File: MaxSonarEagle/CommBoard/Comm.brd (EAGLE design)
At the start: 160 x 100 mm, 1 part

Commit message: schematic updates
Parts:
- added S1, S2: (no value), SparkFun-Switches:DIPSWITCH-08
- added U$1, U$2, U$3, U$4, U$5, U$6, U$7, U$8: LV-MAXSONAR-EZ, Comm:1X07
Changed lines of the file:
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@@
 <layer number="230" name="230bmp" color="7" fill="1" visible="yes" active="yes"/>
 <layer number="231" name="231bmp" color="7" fill="1" visible="yes" active="yes"/>
+<layer number="232" name="Eagle3D_PG2" color="7" fill="1" visible="no" active="no"/>
+<layer number="233" name="Eagle3D_PG3" color="7" fill="1" visible="no" active="no"/>
 <layer number="248" name="Housing" color="7" fill="1" visible="yes" active="yes"/>
 <layer number="249" name="Edge" color="7" fill="1" visible="yes" active="yes"/>
@@
 <elements>
 <element name="FRAME1" library="SparkFun-Aesthetics" package="CREATIVE_COMMONS" value="FRAME-LEDGER" x="21.59" y="-8.89"/>
+<element name="U$1" library="Comm" package="1X07" value="LV-MAXSONAR-EZ" x="10.16" y="-20.32"/>
+<element name="U$2" library="Comm" package="1X07" value="LV-MAXSONAR-EZ" x="10.16" y="-39.37"/>
+<element name="U$3" library="Comm" package="1X07" value="LV-MAXSONAR-EZ" x="10.16" y="-58.42"/>
+<element name="U$4" library="Comm" package="1X07" value="LV-MAXSONAR-EZ" x="10.16" y="-77.47"/>
+<element name="U$5" library="Comm" package="1X07" value="LV-MAXSONAR-EZ" x="10.16" y="-96.52"/>
+<element name="U$6" library="Comm" package="1X07" value="LV-MAXSONAR-EZ" x="10.16" y="-115.57"/>
+<element name="U$7" library="Comm" package="1X07" value="LV-MAXSONAR-EZ" x="10.16" y="-134.62"/>
+<element name="U$8" library="Comm" package="1X07" value="LV-MAXSONAR-EZ" x="10.16" y="-153.67"/>
+<element name="S1" library="SparkFun-Switches" package="DIPSWITCH-08" value="" x="16.51" y="-175.26">
+<attribute name="PROD_ID" value="SWCH-12197" x="16.51" y="-175.26" size="1.778" layer="27" display="off"/>
+<attribute name="SF_SKU" value="COM-08034" x="16.51" y="-175.26" size="1.778" layer="27" display="off"/>
+</element>
+<element name="S2" library="SparkFun-Switches" package="DIPSWITCH-08" value="" x="16.51" y="-198.12">
+<attribute name="PROD_ID" value="SWCH-12197" x="16.51" y="-198.12" size="1.778" layer="27" display="off"/>
+<attribute name="SF_SKU" value="COM-08034" x="16.51" y="-198.12" size="1.778" layer="27" display="off"/>
+</element>
 </elements>
 <signals>

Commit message: finalized board
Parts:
- removed S1: (no value), SparkFun-Switches:DIPSWITCH-08
- added D1, D11, D13, D15, D3, D33, D37, D5, D7, D9: (no value), SparkFun-LED:LED-0603
- added H1, H2, H3, H4: STAND-OFF, SparkFun-Hardware:STAND-OFF
- added J2: (no value), SparkFun-Connectors:MOLEX-1X6
- added Q1, Q10, Q19, Q2, Q21, Q22, Q23, Q24, Q25, Q26, Q27, Q3, Q4, Q5, Q6, Q7, Q8, Q9: 2N3904, SparkFun-DiscreteSemi:SOT23-3
- added R1, R11, R13, R15, R3, R33, R5, R7, R9: 50, SparkFun-Resistors:0805
- added R10, R12, R14, R16, R17, R18, R2, R38, R4, R42, R44, R46, R48, R50, R52, R54, R6, R8: 1k, SparkFun-Resistors:0805
- added R19, R49: 10k, SparkFun-Resistors:0805
- added R37: 350, SparkFun-Resistors:0805
- added U1, U2: 74HC1G04, SparkFun-IC-Logic:SOT353
- moved S2 241.2 mm to (71.1, 36.8), turned to 270 degrees
- moved U$8 186.7 mm to (58.4, 26.7), turned to 270 degrees
- moved U$7 166.3 mm to (50.8, 26.7), turned to 270 degrees
- moved U$6 146.0 mm to (43.2, 26.7), turned to 270 degrees
- moved U$5 125.8 mm to (35.6, 26.7), turned to 270 degrees
- moved U$4 105.6 mm to (27.9, 26.7), turned to 270 degrees
- moved FRAME1 92.0 mm to (99.1, 40.6), turned to 180 degrees
- moved U$3 85.7 mm to (20.3, 26.7), turned to 270 degrees
- moved U$2 66.1 mm to (12.7, 26.7), turned to 270 degrees
- moved U$1 47.3 mm to (5.08, 26.7), turned to 270 degrees
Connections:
- new net GND: J2.1, Q1.2, Q10.2, Q3.2, Q4.2, Q5.2, Q6.2, Q7.2, Q8.2, Q9.2, R19.1, R37.1, R49.1, U$1.1, U$1.7, U$2.1, U$2.7, U$3.1, U$3.7, U$4.1, U$4.7, U$5.1, U$5.7, U$6.1, U$6.7, U$7.1, U$7.7, U$8.1, U$8.7, U1.3, U2.3
- new net IO-UART-RX: J2.5, U1.4
- new net IO-UART-TX: J2.4, U2.2
- new net IOTX: Q2.2, R19.2, R2.1, S2.1, U$1.4
- new net N$1: D1.C, R1.2
- new net N$10: Q6.3, R9.1
- new net N$11: D11.C, R11.2
- new net N$12: Q7.3, R11.1
- new net N$13: D13.C, R13.2
- new net N$14: Q8.3, R13.1
- new net N$15: D15.C, R15.2
- new net N$16: Q9.3, R15.1
- new net N$17: Q2.1, R17.2
- new net N$18: Q10.3, R33.1
- new net N$2: Q1.3, R1.1
- new net N$20: Q10.1, R2.2
- new net N$22: Q9.1, R4.2
- new net N$24: Q8.1, R6.2
- new net N$26: Q7.1, R8.2
- new net N$28: Q6.1, R10.2
- new net N$3: D3.C, R3.2
- new net N$30: Q5.1, R12.2
- new net N$32: Q1.1, R14.2
- new net N$33: D33.C, R33.2
- new net N$34: Q3.1, R16.2
- new net N$37: D37.C, R37.2
- new net N$38: Q19.1, R38.2
- new net N$4: Q3.3, R3.1
- new net N$5: D5.C, R5.2
- new net N$6: Q4.3, R5.1
- new net N$61: Q21.1, R42.2
- new net N$63: Q4.1, R18.2
- new net N$65: Q22.1, R44.2
- new net N$68: Q23.1, R46.2
- new net N$7: D7.C, R7.2
- new net N$71: Q24.1, R48.2
- new net N$74: Q25.1, R50.2
- new net N$77: Q26.1, R52.2
- new net N$8: Q5.3, R7.1
- new net N$80: Q27.1, R54.2
- new net N$9: D9.C, R9.2
- new net RS232-RX: Q19.2, Q21.2, Q22.2, Q23.2, Q24.2, Q25.2, Q26.2, Q27.2, R49.2, U1.2
- new net RS232-TX: R17.1, U2.4
- new net TX1: R14.1, R38.1, S2.16, S2.2, U$1.3, U$2.4
- new net TX2: R16.1, R42.1, S2.15, S2.3, U$2.3, U$3.4
- new net TX3: R18.1, R44.1, S2.14, S2.4, U$3.3, U$4.4
- new net TX4: R12.1, R46.1, S2.13, S2.5, U$4.3, U$5.4
- new net TX5: R10.1, R48.1, S2.12, S2.6, U$5.3, U$6.4
- new net TX6: R50.1, R8.1, S2.11, S2.7, U$6.3, U$7.4
- new net TX7: R52.1, R6.1, S2.10, S2.8, U$7.3, U$8.4
- new net TX8: R4.1, R54.1, S2.9, U$8.3
- new net VIN: D1.A, D11.A, D13.A, D15.A, D3.A, D33.A, D37.A, D5.A, D7.A, D9.A, J2.3, Q19.3, Q2.3, Q21.3, Q22.3, Q23.3, Q24.3, Q25.3, Q26.3, Q27.3, U$1.2, U$2.2, U$3.2, U$4.2, U$5.2, U$6.2, U$7.2, U$8.2, U1.5, U2.5
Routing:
- net IOTX: track 0.00 -> 230.1 mm
- net VIN: track 0.00 -> 183.6 mm, vias 0 -> 14
- net TX1: track 0.00 -> 132.4 mm
- net RS232-RX: track 0.00 -> 130.8 mm, vias 0 -> 2
- net TX2: track 0.00 -> 100.0 mm
- net TX3: track 0.00 -> 93.8 mm
- net TX4: track 0.00 -> 88.8 mm
- net TX5: track 0.00 -> 81.7 mm, vias 0 -> 1
- net TX6: track 0.00 -> 74.9 mm
- net TX7: track 0.00 -> 70.0 mm
- net TX8: track 0.00 -> 59.3 mm, vias 0 -> 3
- net GND: track 0.00 -> 51.4 mm, vias 0 -> 10
- net RS232-TX: track 0.00 -> 12.3 mm
- net N$16: track 0.00 -> 11.8 mm
- net N$14: track 0.00 -> 10.6 mm
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- added copper zone on layer 16, net GND
- added copper zone on layer 1, net VIN
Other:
- board size 160 x 100 mm -> 102.8 x 54.3 mm
- board text added: "+"
- board text added: "1"
- board text added: "1 2 3 4 5 6 7 8"
- board text added: "2"
- board text added: "3"
- board text added: "4"
- board text added: "5"
- board text added: "6"
- board text added: "7"
- board text added: "8"
- board text added: "GND"
- board text added: "IO"
- board text added: "S1 S2 S3 S4 S5 S6 S7 S8"
- board text added: "Sonar Communications Board v1.0"
- board text added: "TX Bridge"

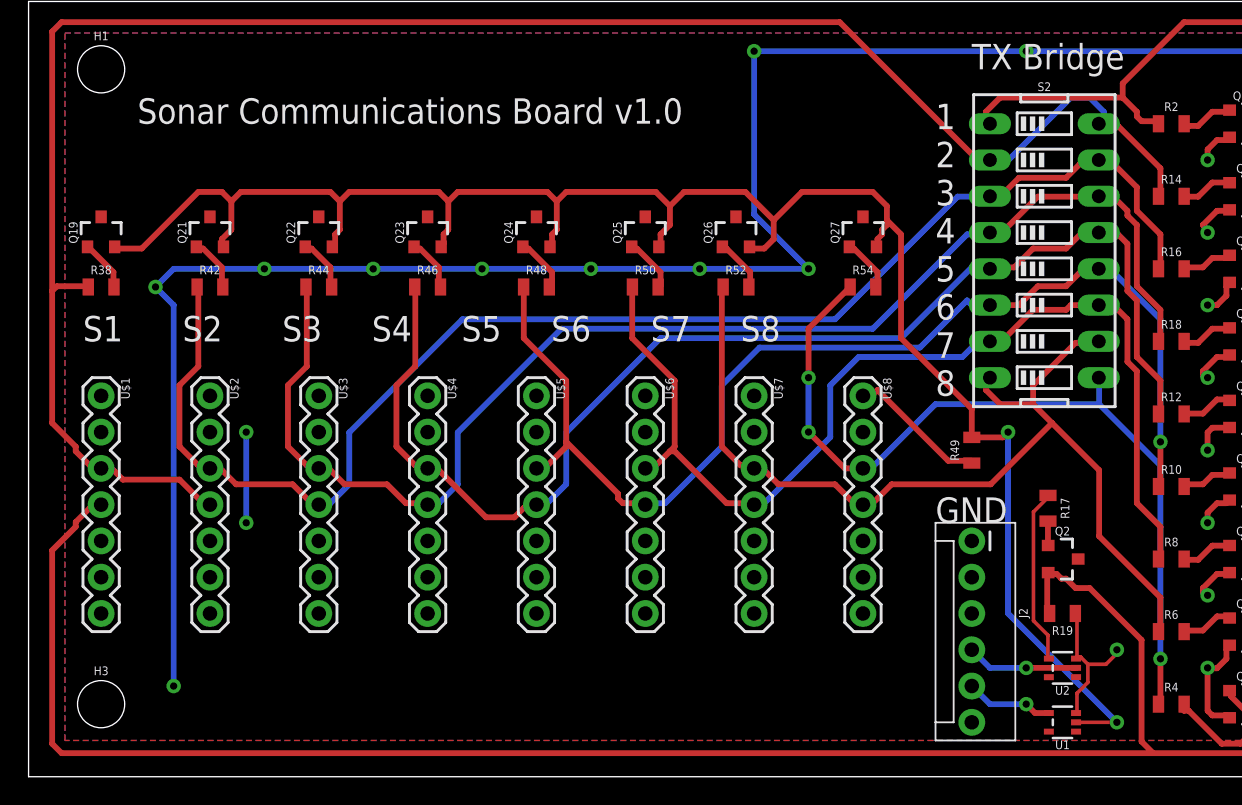
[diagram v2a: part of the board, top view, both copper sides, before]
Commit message: added pulldown resistors to sonar rx lines
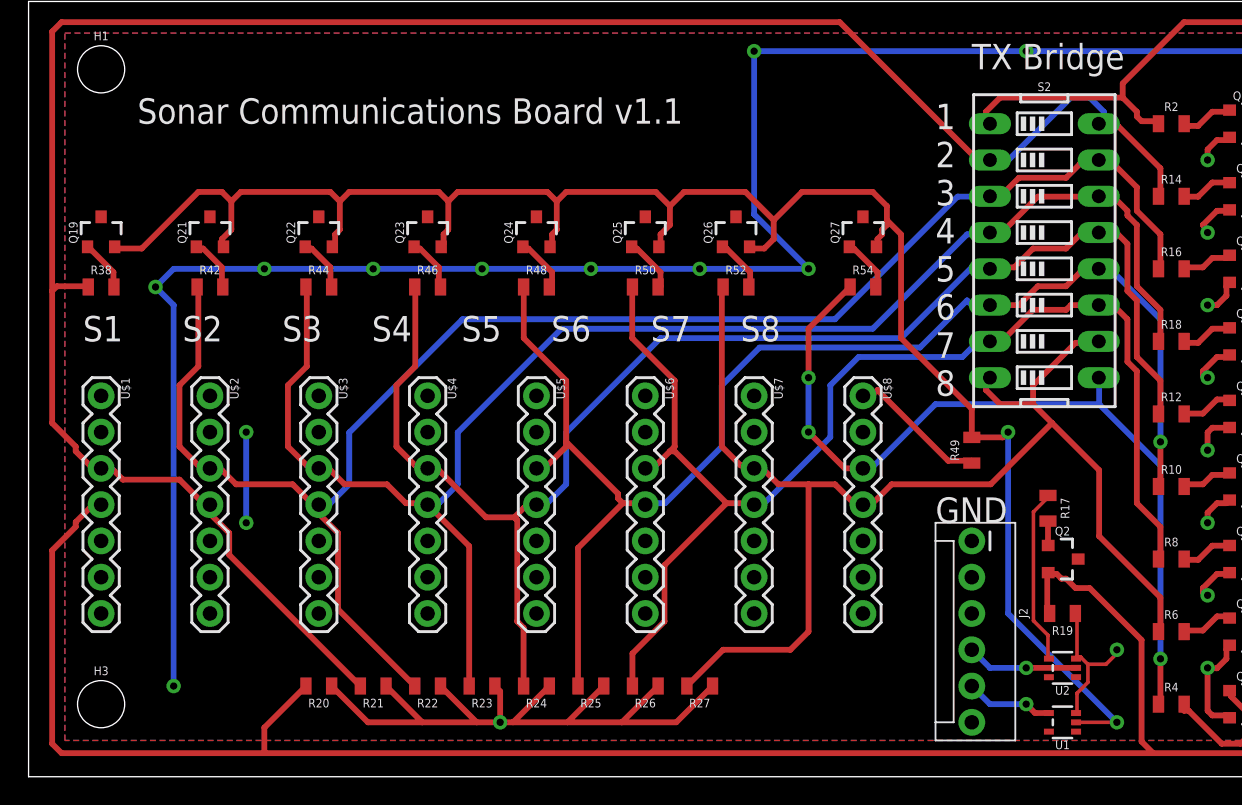
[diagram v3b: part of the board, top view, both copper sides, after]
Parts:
- added R20, R21, R22, R23, R24, R25, R26, R27: 10k, SparkFun-Resistors:0805
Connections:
- net GND: now also R20.1, R21.1, R22.1, R23.1, R24.1, R25.1, R26.1, R27.1
- net IOTX: now also R20.2
- net TX1: now also R21.2
- net TX2: now also R22.2
- net TX3: now also R23.2
- net TX4: now also R24.2
- net TX5: now also R25.2
- net TX6: now also R26.2
- net TX7: now also R27.2
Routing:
- net GND: track 51.4 -> 100.8 mm, vias 10 -> 11
- net TX7: track 70.0 -> 90.4 mm
- net TX1: track 132.4 -> 149.5 mm
- net TX6: track 74.9 -> 90.4 mm
- net TX2: track 100.0 -> 115.5 mm
- net TX5: track 81.7 -> 95.8 mm
- net TX3: track 93.8 -> 107.7 mm
- net TX4: track 88.8 -> 100.8 mm
- net IOTX: track 230.1 -> 236.0 mm
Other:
- board text added: "Sonar Communications Board v1.1"
- board text removed: "Sonar Communications Board v1.0"
